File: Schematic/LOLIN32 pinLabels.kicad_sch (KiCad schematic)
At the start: 40 parts

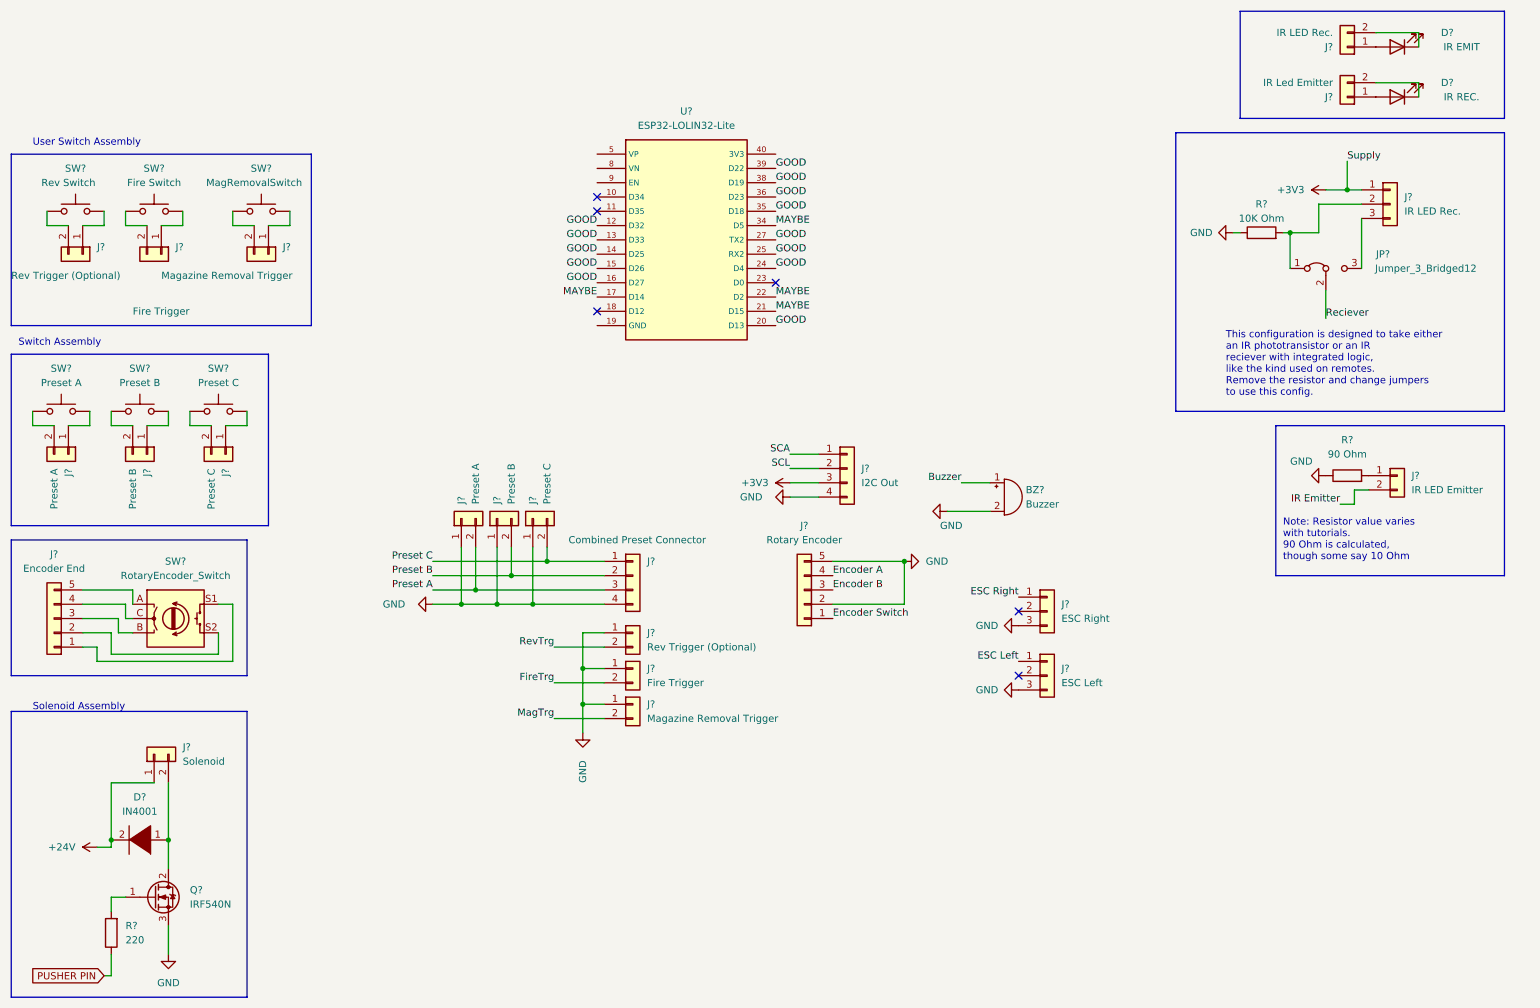
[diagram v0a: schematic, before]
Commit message: update PCB model
progress on logic-side board
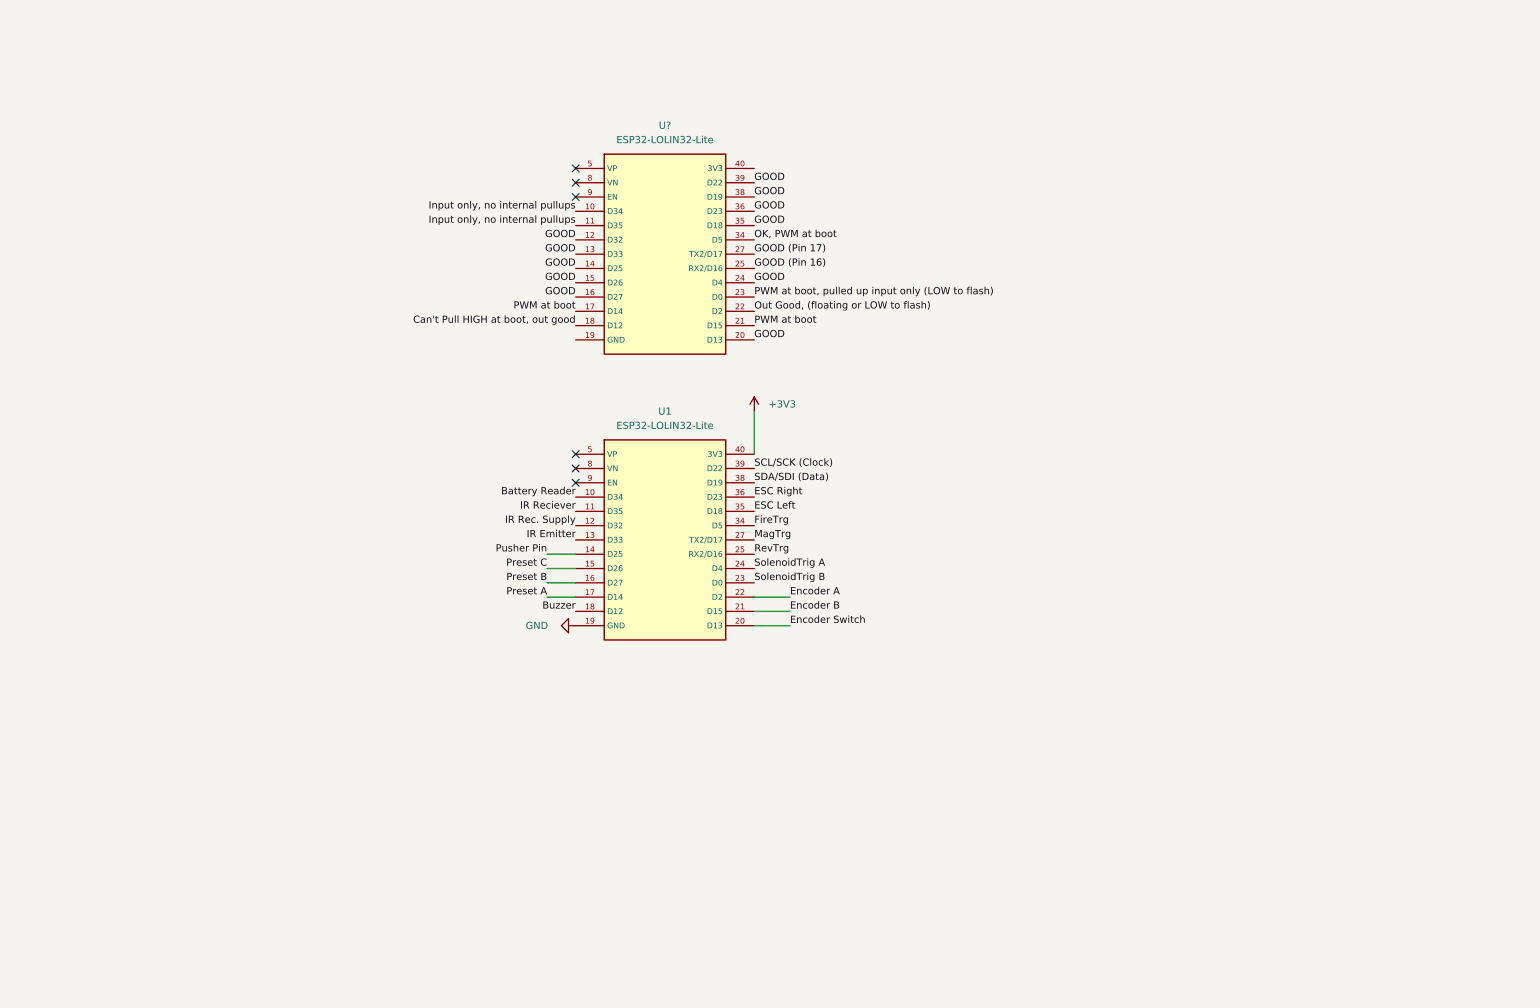
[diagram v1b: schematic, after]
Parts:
- removed BZ?: Buzzer, symbol Device:Buzzer
- removed D?: IN4001, Diode_THT:D_DO-41_SOD81_P7.62mm_Horizontal, symbol pspice:DIODE
- removed D?: IR EMIT, symbol Device:LED
- removed D?: IR REC., symbol Device:LED
- removed J? (x2): Magazine Removal Trigger, symbol Connector_Generic:Conn_01x02
- removed J?: IR LED Emitter, symbol Connector_Generic:Conn_01x02
- removed J?: IR LED Rec., symbol Connector_Generic:Conn_01x02
- removed J? (x2): Fire Trigger, symbol Connector_Generic:Conn_01x02
- removed J? (x2): Preset C, symbol Connector_Generic:Conn_01x02
- removed J?: Rotary Encoder, symbol Connector_Generic:Conn_01x05
- removed J?: ESC Right, Connector_PinHeader_2.54mm:PinHeader_1x03_P2.54mm_Vertical, symbol Connector_Generic:Conn_01x03
- removed J? (x2): Rev Trigger (Optional), symbol Connector_Generic:Conn_01x02
- removed J?: IR Led Emitter, symbol Connector_Generic:Conn_01x02
- removed J? (x2): Preset B, symbol Connector_Generic:Conn_01x02
- removed J?: I2C Out, symbol Connector_Generic:Conn_01x04
- removed J?: Solenoid, Connector_PinHeader_2.54mm:PinHeader_1x02_P2.54mm_Vertical, symbol Connector_Generic:Conn_01x02
- removed J?: Encoder End, symbol Connector_Generic:Conn_01x05
- removed J?: Combined Preset Connector, symbol Connector_Generic:Conn_01x04
- removed J? (x2): Preset A, symbol Connector_Generic:Conn_01x02
- removed J?: ESC Left, symbol Connector_Generic:Conn_01x03
- removed J?: IR LED Rec., Connector_PinHeader_2.54mm:PinHeader_1x03_P2.54mm_Vertical, symbol Connector_Generic:Conn_01x03
- removed JP?: Jumper_3_Bridged12, symbol Jumper:Jumper_3_Bridged12
- removed Q?: IRF540N, Package_TO_SOT_THT:TO-220-3_Vertical, symbol Transistor_FET:IRF540N
- removed R?: 220, Resistor_THT:R_Axial_DIN0207_L6.3mm_D2.5mm_P7.62mm_Horizontal, symbol Device:R
- removed R?: 10K Ohm, symbol Device:R
- removed R?: 90 Ohm, symbol Device:R
- removed SW?: Preset A, symbol Switch:SW_Push
- removed SW?: Preset C, symbol Switch:SW_Push
- removed SW?: Fire Switch, symbol Switch:SW_Push
- removed SW?: Preset B, symbol Switch:SW_Push
- removed SW?: Rev Switch, symbol Switch:SW_Push
- removed SW?: MagRemovalSwitch, symbol Switch:SW_Push
- removed SW?: RotaryEncoder_Switch, symbol Device:RotaryEncoder_Switch
- added U1: ESP32-LOLIN32-Lite, Espressif:ESP32-LOLIN32-Lite, symbol Espressif:ESP32-LOLIN32-Lite
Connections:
- net +3V3: now also U1.40 (3V3)
- net Buzzer: now also U1.18 (D12)
- net ESC Left: now also U1.35 (D18)
- net ESC Right: now also U1.36 (D23)
- net Encoder A: now also U1.22 (D2)
- net Encoder B: now also U1.21 (D15)
- net Encoder Switch: now also U1.20 (D13)
- net FireTrg: now also U1.34 (D5)
- net GND: now also U1.19 (GND)
- net GOOD: no longer U?.25 (RX2), U?.27 (TX2)
- net IR Emitter: now also U1.13 (D33)
- net MagTrg: now also U1.27 (TX2/D17)
- net Preset A: now also U1.17 (D14)
- net Preset B: now also U1.16 (D27)
- net Preset C: now also U1.15 (D26)
- net RevTrg: now also U1.25 (RX2/D16)
- net Input only, no internal pullups: now reaches U?.10 (D34)
- net Input only, no internal pullups: now also U?.11 (D35)
- net Can't Pull HIGH at boot, out good: now reaches U?.18 (D12)
- net PWM at boot, pulled up input only (LOW to flash): now reaches U?.23 (D0)
- net MAYBE renamed PWM at boot
- net PWM at boot: no longer U?.22 (D2), U?.34 (D5)
- new net Battery Reader: U1.10 (D34)
- new net GOOD (Pin 16): U?.25 (RX2/D16)
- new net GOOD (Pin 17): U?.27 (TX2/D17)
- new net IR Rec. Supply: U1.12 (D32)
- new net IR Reciever: U1.11 (D35)
- new net OK, PWM at boot: U?.34 (D5)
- new net Out Good, (floating or LOW to flash): U?.22 (D2)
- new net Pusher Pin: U1.14 (D25)
- new net SCL/SCK (Clock): U1.39 (D22)
- new net SDA/SDI (Data): U1.38 (D19)
- new net SolenoidTrig A: U1.24 (D4)
- new net SolenoidTrig B: U1.23 (D0)
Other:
- note removed: "Note: Resistor value varies with tutorials. 90 Ohm is calculated, though some say 10 Ohm"
- note removed: "Solenoid Assembly"
- note removed: "Switch Assembly"
- note removed: "This configuration is designed to take either an IR phototransistor or an IR reciever with integrated logic, like the kind used on remotes. Remove the resistor and change jumpers to use this config."
- note removed: "User Switch Assembly"
- moved on the sheet: U?
